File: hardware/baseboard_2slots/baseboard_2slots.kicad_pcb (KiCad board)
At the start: 2 copper layers, 216.8 x 60 mm, 43 parts, among them J1 IO-Board_00, J10 Conn_01x04_Male, J11 Conn_01x04_Male, J12 Conn_01x04_Male, J13 Conn_01x04_Male, J14 Conn_01x04_Male, J15 Conn_02x02_Odd_Even, J2 IO-Board_01, J5 USB_B_Micro, J6 Conn_01x05: Adafruit 1833, J7 Screw_Terminal_01x04, J8 Conn_02x02_Odd_Even, J9 Conn_02x02_Odd_Even, U1 NRF24L01_Breakout, U2 Pico, U3 W5500_Mini

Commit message: Fix DRC errors
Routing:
- net +3.3V: vias 9 -> 8
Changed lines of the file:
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@@
   (segment (start 235.536 31.888) (end 235.058 32.366) (width 0.45) (layer "F.Cu") (net 1))
   (segment (start 235.058 32.366) (end 233.026 32.366) (width 0.45) (layer "F.Cu") (net 1))
-  (segment (start 147.682 80.048) (end 147.73 80) (width 1) (layer "F.Cu") (net 1))
   (segment (start 235.536 30.71) (end 235.536 31.888) (width 0.45) (layer "F.Cu") (net 1))
   (segment (start 233.026 32.366) (end 233.026 30.745) (width 0.45) (layer "F.Cu") (net 1))
@@
   (via (at 111.5 67.5) (size 0.8) (drill 0.4) (layers "F.Cu" "B.Cu") (net 3))
   (via (at 221.596 54.5) (size 0.8) (drill 0.4) (layers "F.Cu" "B.Cu") (net 3))
-  (via (at 268.586 60.814) (size 0.8) (drill 0.4) (layers "F.Cu" "B.Cu") (net 3))
   (via (at 140.316 62.3) (size 0.8) (drill 0.4) (layers "F.Cu" "B.Cu") (net 3))
   (via (at 268.4 70.2) (size 0.8) (drill 0.4) (layers "F.Cu" "B.Cu") (net 3))

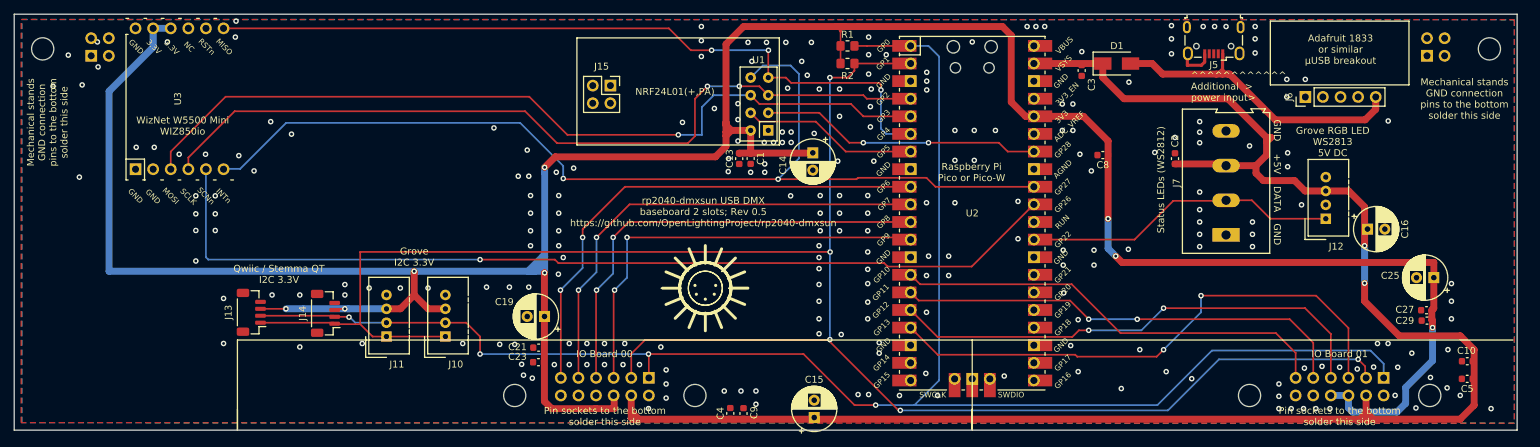
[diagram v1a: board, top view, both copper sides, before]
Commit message: Add a IRQ config jumper for the nRF24 and the Wiz modules
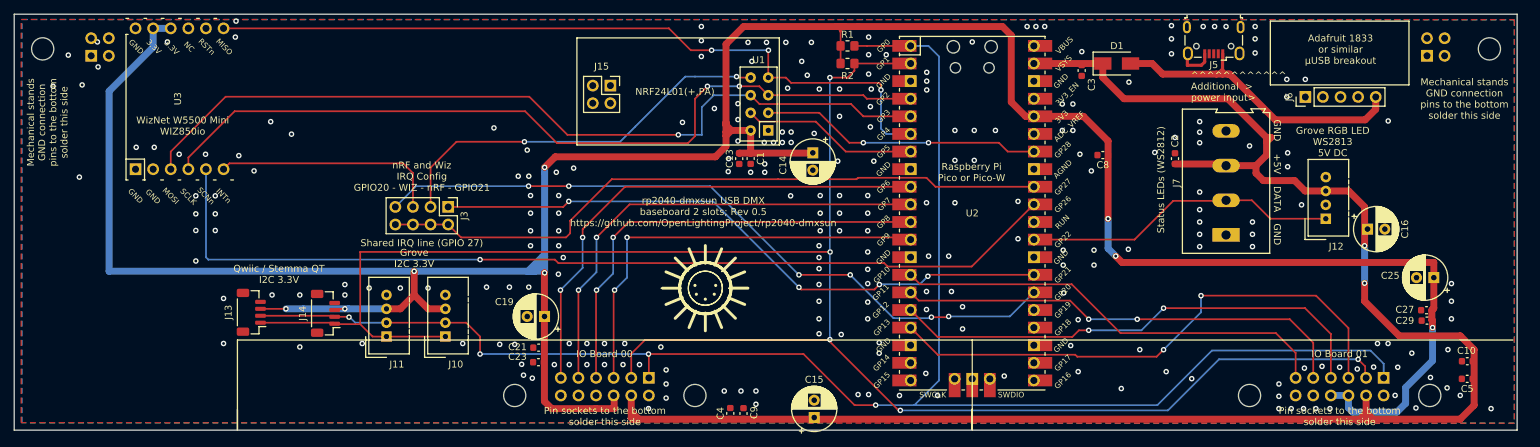
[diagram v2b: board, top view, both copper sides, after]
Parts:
- added J3: Conn_02x04_Odd_Even, Connector_PinHeader_2.54mm:PinHeader_2x04_P2.54mm_Vertical, F.Cu at (126.4, 52.8)
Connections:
- U1 pad 8: /WIZ_NRF_INT -> /INT_RF24
- U2 pad 19: /IO2_GP0 -> unconnected-(U2-Pad19)
- U2 pad 20: /IO2_GP1 -> unconnected-(U2-Pad20)
- U2 pad 21: /IO2_GP2 -> unconnected-(U2-Pad21)
- U2 pad 22: /IO2_GP3 -> unconnected-(U2-Pad22)
- U2 pad 24: /IO3_GP0 -> unconnected-(U2-Pad24)
- U2 pad 25: /IO3_GP1 -> unconnected-(U2-Pad25)
- U2 pad 26: /IO3_GP2 -> Net-(U2-Pad26)
- U2 pad 27: /IO3_GP3 -> Net-(U2-Pad27)
- U3 pad 6: /WIZ_NRF_INT -> /INT_WIZ
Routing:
- net Net-(U2-Pad26): track 0.00 -> 102.8 mm, vias 0 -> 6
- net Net-(U2-Pad27): track 0.00 -> 91.0 mm, vias 0 -> 4
- net /INT_RF24: track 0.00 -> 57.3 mm, vias 0 -> 2
- net /WIZ_NRF_INT: track 149.1 -> 98.0 mm, vias 2 -> 0
- net /INT_WIZ: track 0.00 -> 33.1 mm
- net GND: vias 248 -> 250
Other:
- board text added: "Shared IRQ line (GPIO 27)"
- board text added: "nRF and Wiz IRQ Config GPIO20 - WIZ - nRF - GPIO21"

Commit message: Bump all boards to rev 0.6
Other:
- board text added: "rp2040-dmxsun USB DMX baseboard 2 slots; Rev 0.6 https://github.com/OpenLightingProject/rp2040-dmxsun"
- board text removed: "rp2040-dmxsun USB DMX baseboard 2 slots; Rev 0.5 https://github.com/OpenLightingProject/rp2040-dmxsun"
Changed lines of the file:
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@@
     (effects (font (size 1 1) (thickness 0.15)))
   )
-  (gr_text "rp2040-dmxsun USB DMX\nbaseboard 2 slots; Rev 0.5\nhttps://github.com/OpenLightingProject/rp2040-dmxsun" (at 163.2 53.5) (layer "F.SilkS")
+  (gr_text "rp2040-dmxsun USB DMX\nbaseboard 2 slots; Rev 0.6\nhttps://github.com/OpenLightingProject/rp2040-dmxsun" (at 163.2 53.5) (layer "F.SilkS")
     (effects (font (size 1 1) (thickness 0.15)))
   )

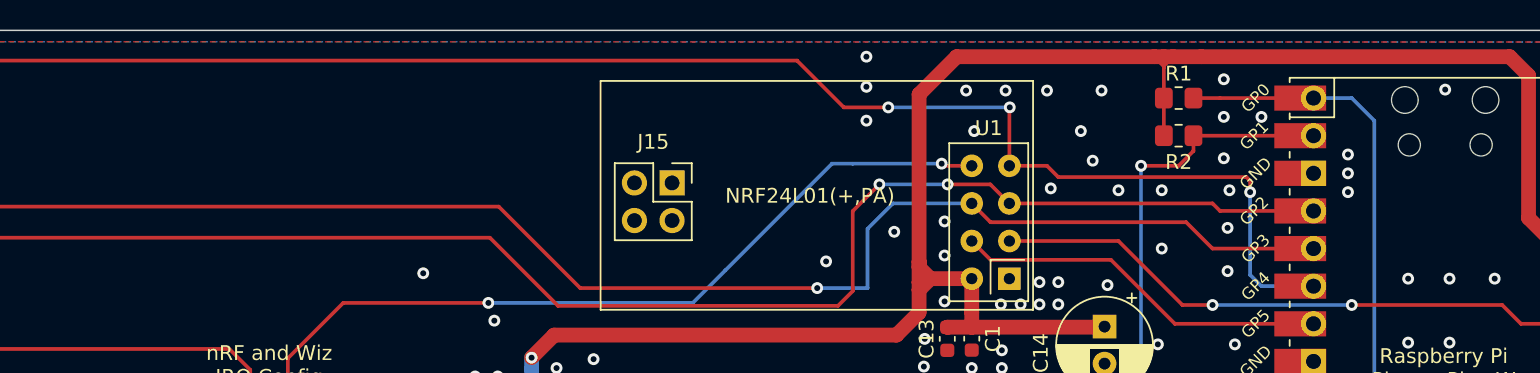
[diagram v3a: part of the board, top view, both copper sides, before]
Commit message: Update baseboards to KiCad 8, add copper keepout underneath Picos, add OpenHardware logo
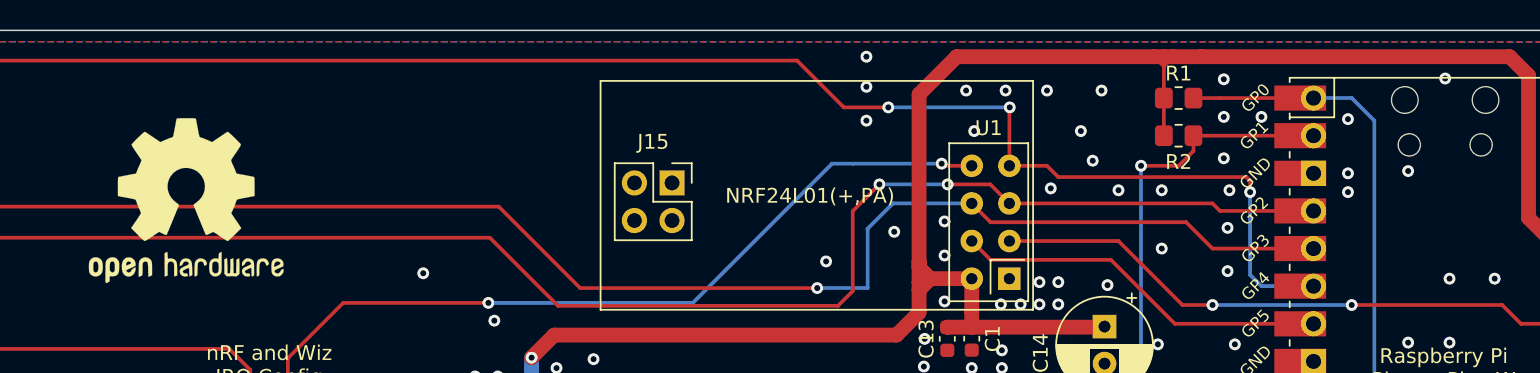
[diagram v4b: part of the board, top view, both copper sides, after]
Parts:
- added SYM1: Logo_Open_Hardware_Large, Symbol:OSHW-Logo2_14.6x12mm_SilkScreen, F.Cu at (117.0, 36.5)

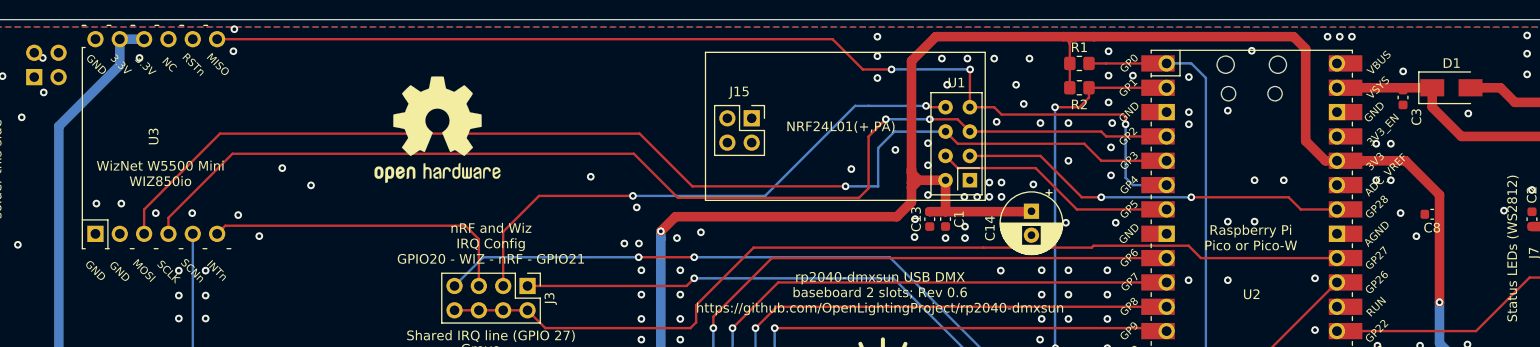
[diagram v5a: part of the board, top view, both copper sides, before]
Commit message: Update all footprints and ignore all other DRC warning on baseboards
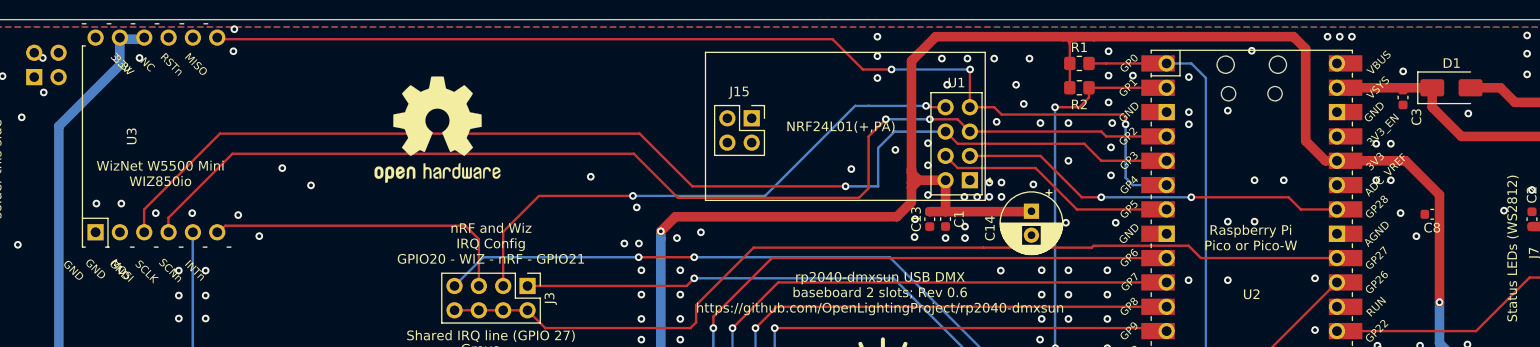
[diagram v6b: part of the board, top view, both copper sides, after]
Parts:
- U3: value W5500_Mini -> W5500_Mini_TH
- moved U3 2.29 mm to (85.1, 37.2)
